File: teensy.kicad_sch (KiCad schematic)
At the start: 29 parts, among them J1 Conn_01x02, J2 ESP PROG, J3 Conn_01x01, J4 Conn_01x01, J5 Conn_01x01, J6 Conn_01x08, SW1 SW_Push, SW2 SW_SPDT, U1 Teensy4.0, U2 ESP32-C3-DevKitM-1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

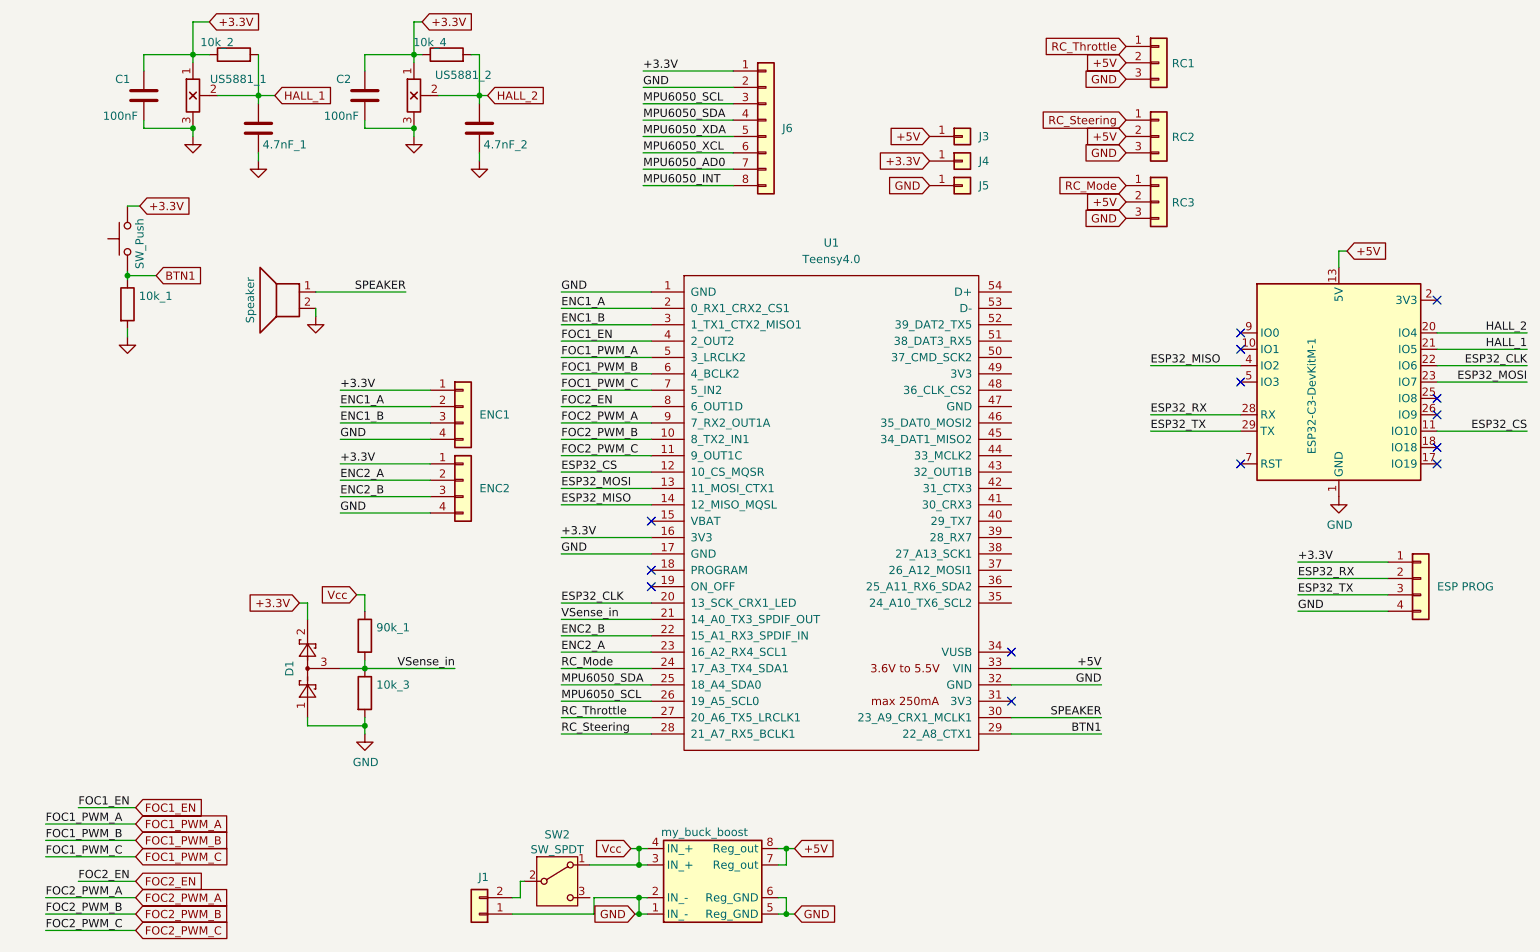
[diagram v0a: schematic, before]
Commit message: added DRV8313
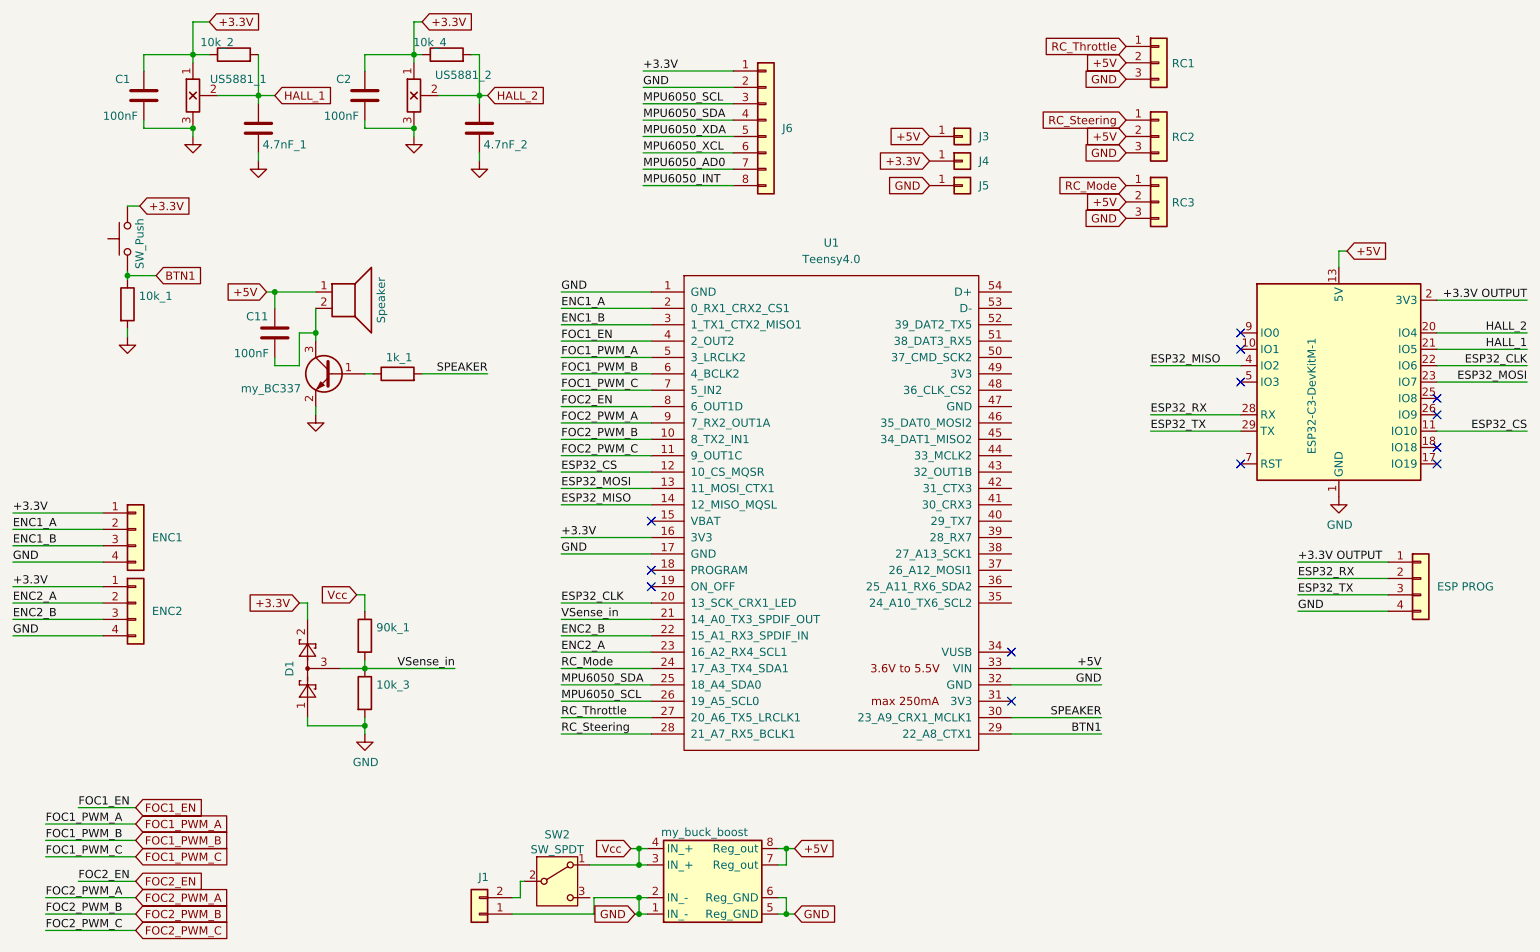
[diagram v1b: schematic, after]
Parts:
- added 1k_1: 10k, Resistor_SMD:R_0805_2012Metric, symbol Device:R
- added C11: 100nF, Capacitor_SMD:C_0805_2012Metric, symbol Device:C
- added Q2: my_BC337, Package_TO_SOT_SMD:SOT-23, symbol Transistor_BJT:my_BC337
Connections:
- net +3.3V: no longer J2.1 (Pin_1)
- net +5V: now also LS1.1, C11.1
- net GND: now also Q2.2 (E); no longer LS1.2
- net SPEAKER: now also 1k_1.2; no longer LS1.1
- net +3.3V OUTPUT: now reaches U2.2 (3V3), U2.3 (3V3)
- net +3.3V OUTPUT: now also J2.1 (Pin_1)
- new net: 1k_1.1, Q2.1 (B)
- new net: C11.2, LS1.2, Q2.3 (C)
- no-connect marks 14 -> 13
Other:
- moved on the sheet: ENC1, ENC2
